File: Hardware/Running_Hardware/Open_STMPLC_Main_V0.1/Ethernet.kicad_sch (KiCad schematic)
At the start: 16 parts, among them J1 RJ45_Bel_SI-60062-F, U1 LAN8720A

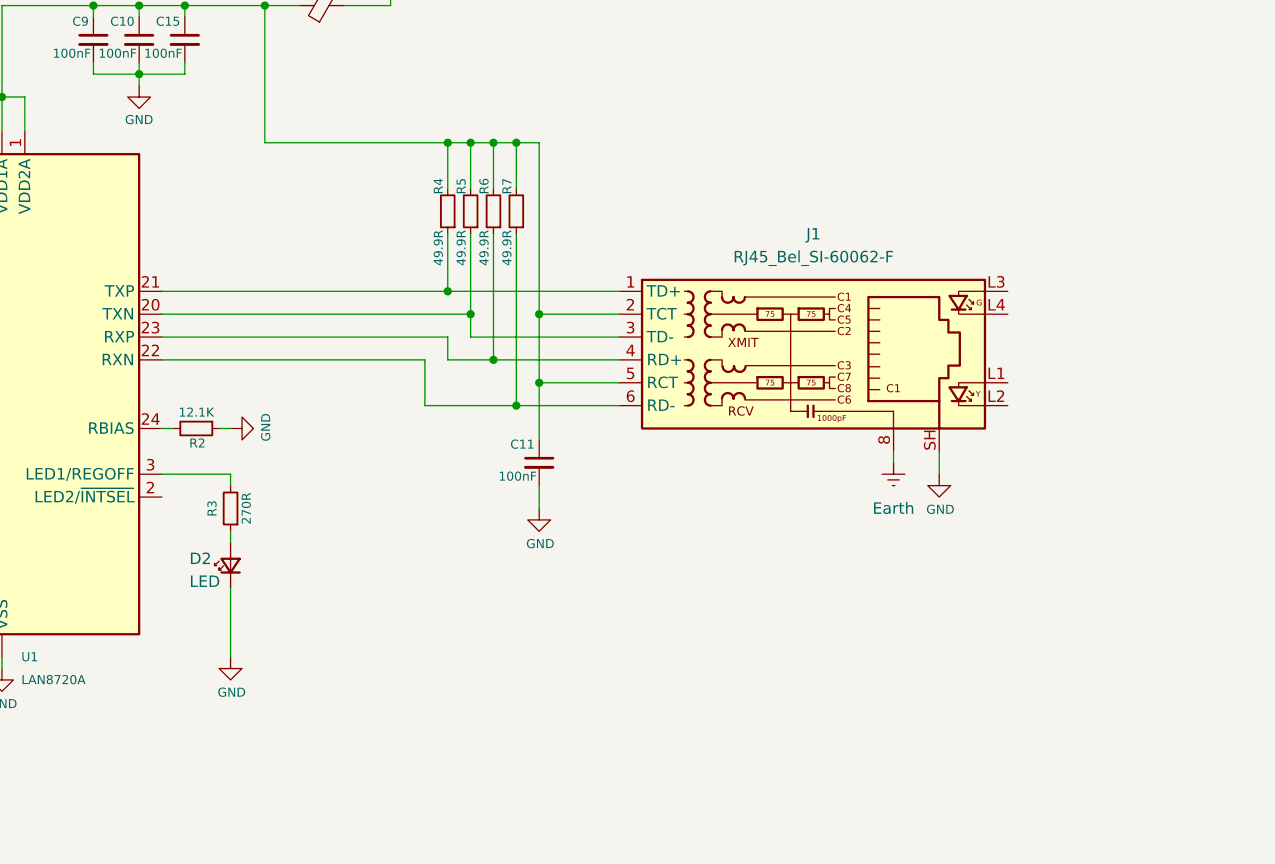
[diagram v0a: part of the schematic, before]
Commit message: GSM Module add
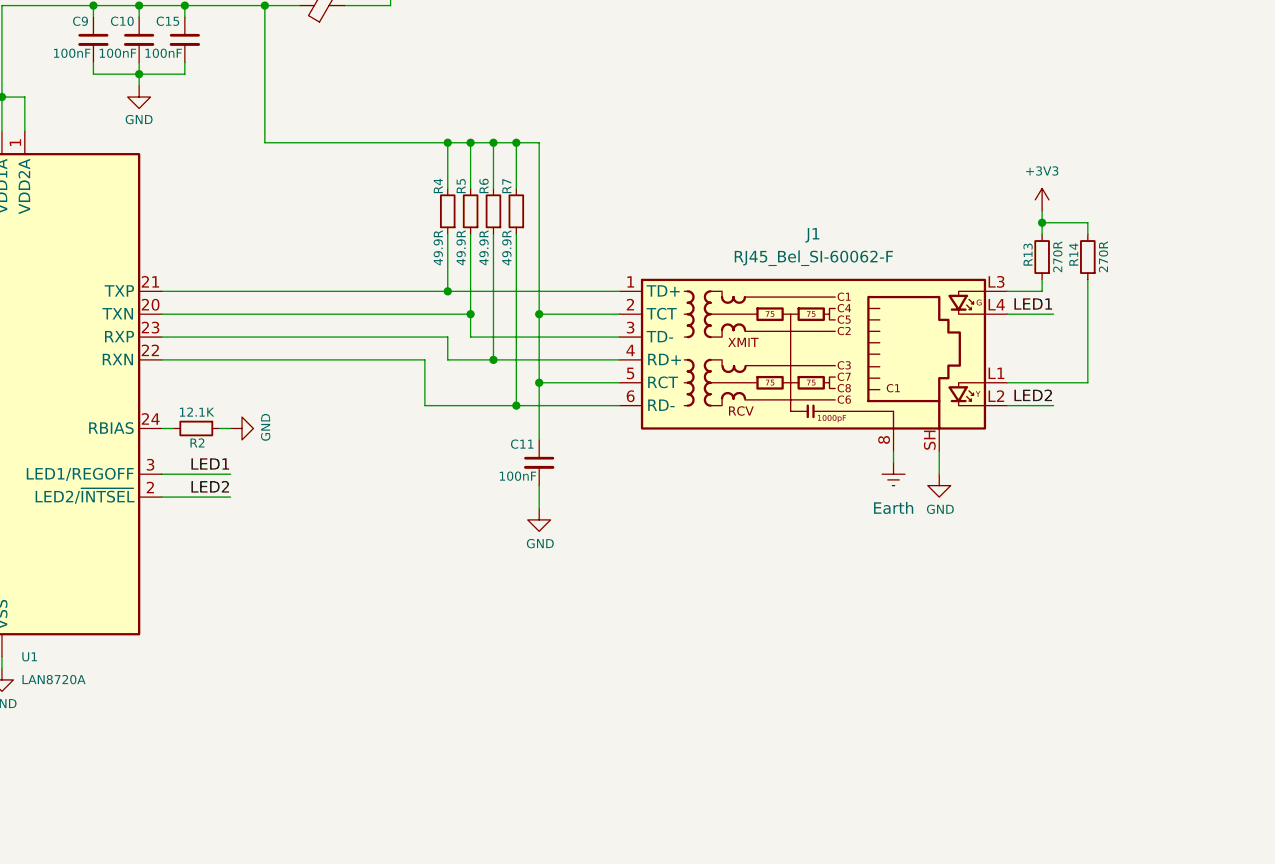
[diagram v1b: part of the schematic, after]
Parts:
- removed D2: LED, symbol Device:LED_Small
- removed R3: 270R, symbol Device:R_Small
- added R13, R14: 270R, Resistor_SMD:R_0603_1608Metric_Pad0.98x0.95mm_HandSolder, symbol Device:R_Small
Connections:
- net +3V3: now also R13.2, R14.2
- net at J1.L1: now also R14.1
- net LED2: now reaches J1.L2
- net LED2: now also U1.2 (LED2/~{INTSEL})
- net at J1.L3: now also R13.1
- net LED1: now reaches J1.L4
- net LED1: now also U1.3 (LED1/REGOFF)

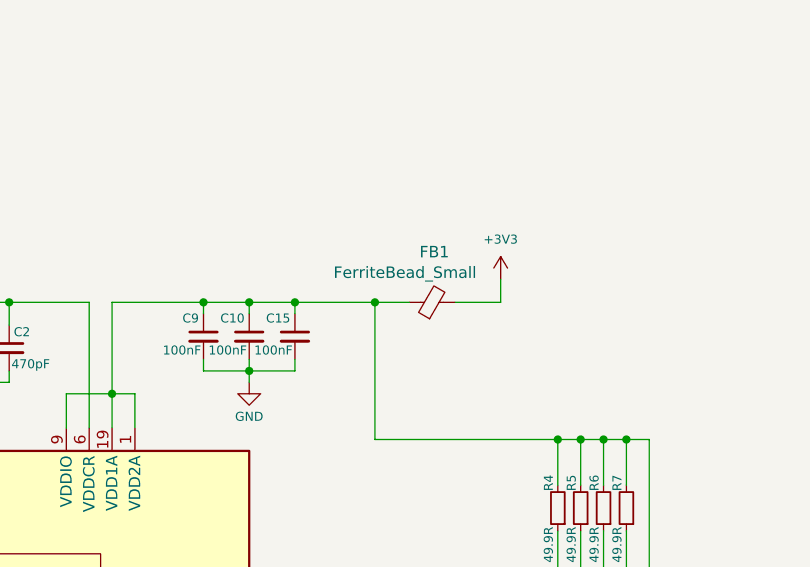
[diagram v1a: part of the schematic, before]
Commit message: Main PCB schematic changes V0.1
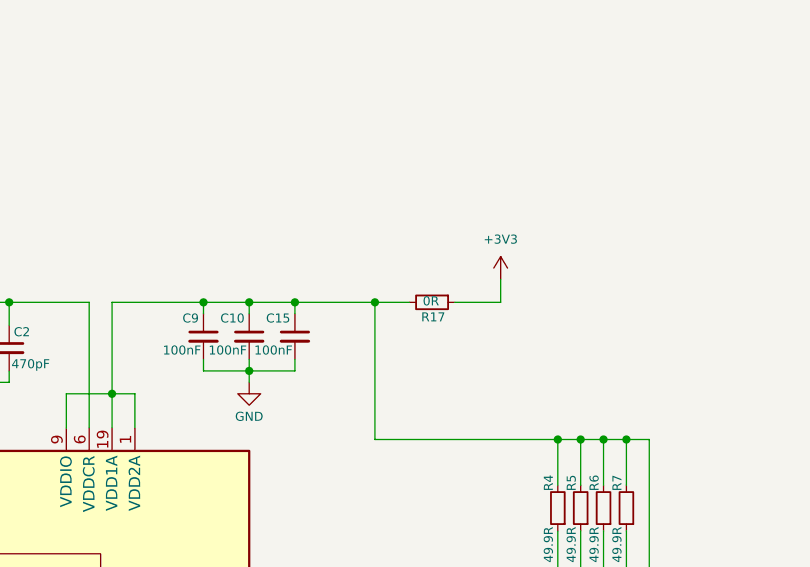
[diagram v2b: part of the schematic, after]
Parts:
- removed FB1: FerriteBead_Small, symbol Device:FerriteBead_Small
- added R17: 0R, Resistor_SMD:R_0603_1608Metric_Pad0.98x0.95mm_HandSolder, symbol Device:R_Small
- C2, C8: footprint (none) -> Capacitor_SMD:C_0603_1608Metric_Pad1.08x0.95mm_HandSolder
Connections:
- net +3V3: now also R17.1
- net at C10.1, C11.1, C15.1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: now also R17.2
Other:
- title: (none) -> Open_STMPLC_Main
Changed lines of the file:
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@@
 	(generator_version "9.0")
 	(paper "A4")
+	(title_block
+		(title "Open_STMPLC_Main")
+		(date "2026-04-04")
+		(rev "0.1")
+	)
 	(rectangle
 		(start 13.97 13.97)
@@
 			)
 		)
-		(property "Footprint" ""
+		(property "Footprint" "Capacitor_SMD:C_0603_1608Metric_Pad1.08x0.95mm_HandSolder"
 			(at 95.25 59.69 0)
 			(effects
@@
 	(symbol
 		(lib_id "Device:R_Small")
+		(at 147.32 54.61 270)
+		(unit 1)
+		(exclude_from_sim no)
+		(in_bom yes)
+		(on_board yes)
+		(dnp no)
+		(property "Reference" "R17"
+			(at 147.447 56.261 90)
+			(effects
+				(font
+					(size 1 1)
+				)
+			)
+		)
+		(property "Value" "0R"
+			(at 147.193 54.483 90)
+			(effects
+				(font
+					(size 1 1)
+				)
+			)
+		)
+		(property "Footprint" "Resistor_SMD:R_0603_1608Metric_Pad0.98x0.95mm_HandSolder"
+			(at 147.32 54.61 0)
+			(effects
+				(font
+					(size 1.27 1.27)
+				)
+				(hide yes)
+			)
+		)
+		(property "Datasheet" "~"
+			(at 147.32 54.61 0)
+			(effects
+				(font
+					(size 1.27 1.27)
+				)
+				(hide yes)
+			)
+		)
+		(property "Description" "Resistor, small symbol"
+			(at 147.32 54.61 0)
+			(effects
+				(font
+					(size 1.27 1.27)
+				)
+				(hide yes)
+			)
+		)
+		(pin "2"
+		)
+		(pin "1"
+		)
+		(instances
+			(project "Open_STMPLC_Main_V0.1"
+				(path "/0b17c9ff-697e-478a-b9b2-a0c5b14c9e6c/2c4ca765-43c3-4f95-8835-dba7f06999bb"
+					(reference "R17")
+					(unit 1)
+				)
+			)
+		)
+	)
+	(symbol
+		(lib_id "Device:R_Small")
 		(at 161.29 77.47 180)
 		(unit 1)
@@
 			)
 		)
-		(property "Footprint" ""
+		(property "Footprint" "Capacitor_SMD:C_0603_1608Metric_Pad1.08x0.95mm_HandSolder"
 			(at 100.33 59.69 0)
 			(effects
@@
 					(unit 1)
 				)
-			)
-		)
-	)
-	(symbol
-		(lib_id "Device:FerriteBead_Small")
-		(at 147.32 54.61 90)
-		(unit 1)
-		(exclude_from_sim no)
-		(in_bom yes)
-		(on_board yes)
-		(dnp no)
-		(property "Reference" "FB1"
-			(at 147.574 49.022 90)
-			(effects
-				(font
-					(size 1.27 1.27)
-				)
-			)
-		)
-		(property "Value" "FerriteBead_Small"
-			(at 144.3101 51.308 90)
-			(effects
-				(font
-					(size 1.27 1.27)
-				)
-			)
-		)
-		(property "Footprint" ""
-			(at 147.32 56.388 90)
-			(effects
-				(font
-					(size 1.27 1.27)
-				)
-				(hide yes)
-			)
-		)
-		(property "Datasheet" "~"
-			(at 147.32 54.61 0)
-			(effects
-				(font
-					(size 1.27 1.27)
-				)
-				(hide yes)
-			)
-		)
-		(property "Description" "Ferrite bead, small symbol"
-			(at 147.32 54.61 0)
-			(effects
-				(font
-					(size 1.27 1.27)
-				)
-				(hide yes)
-			)
-		)
-		(pin "1"
-		)
-		(pin "2"
-		)
-		(instances
-			(project "Open_STMPLC_Main_V0.1"
-				(path "/0b17c9ff-697e-478a-b9b2-a0c5b14c9e6c/2c4ca765-43c3-4f95-8835-dba7f06999bb"
-					(reference "FB1")
-					(unit 1)
-				)

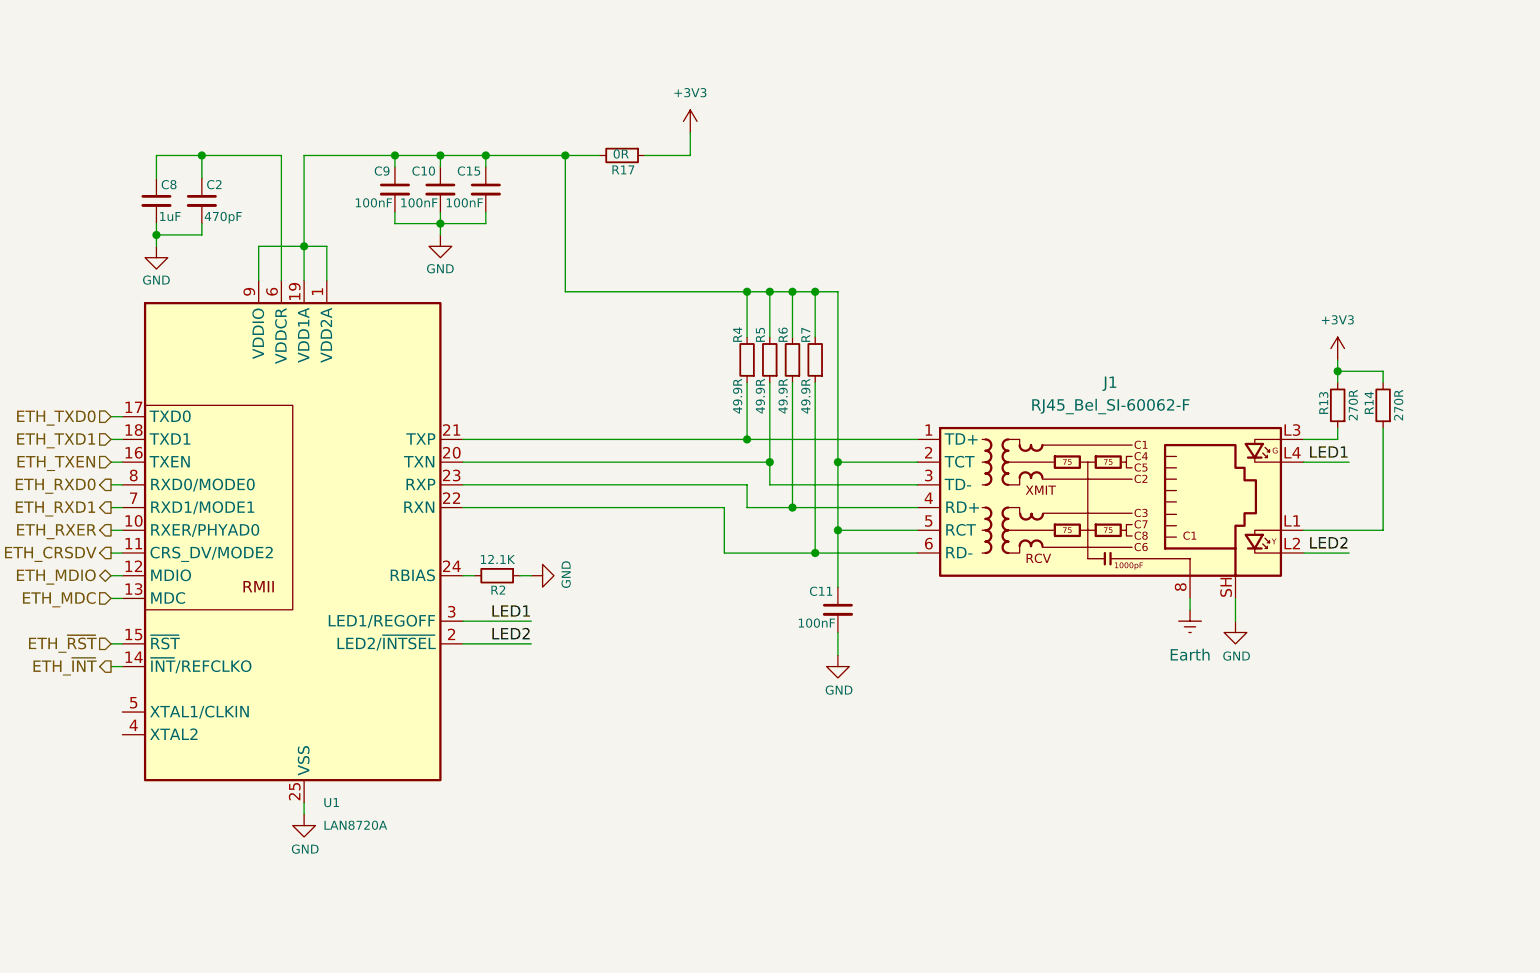
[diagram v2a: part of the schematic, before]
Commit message: Pin mapping IO connector
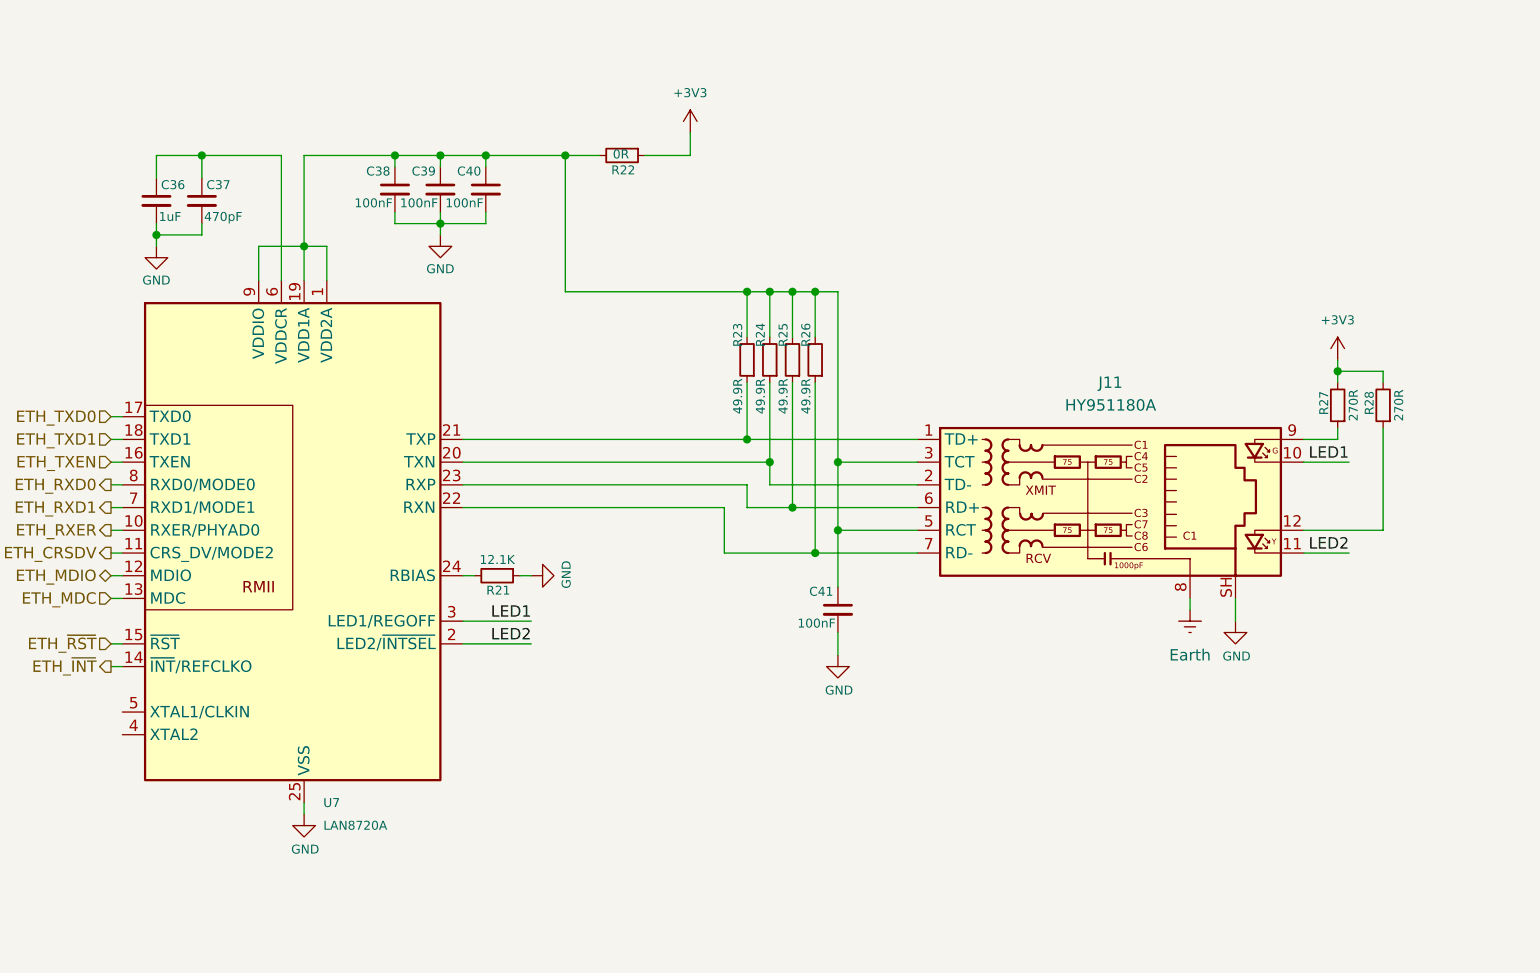
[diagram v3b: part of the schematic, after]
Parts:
- removed J1: RJ45_Bel_SI-60062-F, Connector_RJ:RJ45_Bel_SI-60062-F, symbol Connector:RJ45_Bel_SI-60062-F
- added J11: HY951180A, HY951180A:HY951180A, symbol HY951180A:HY951180A
- renumbered C8 to C36, C2 to C37, C9 to C38, C10 to C39, C15 to C40, C11 to C41, R2 to R21, R17 to R22, R4 to R23, R5 to R24, R6 to R25, R7 to R26, R13 to R27, R14 to R28, U1 to U7
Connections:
- net Earth: now also J11.8
- net GND: now also J11.SH
- net LED1: now also J11.10
- net LED2: now also J11.11
- net at C38.1, C39.1, C40.1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: now also J11.3 (TCT), J11.5 (RCT)
- net at R28.1: now also J11.12
- net at R23.1, U7.21 (TXP): now also J11.1 (TD+)
- net at R24.1, U7.20 (TXN): now also J11.2 (TD-)
- net at R25.1, U7.23 (RXP): now also J11.6 (RD+)
- net at R26.1, U7.22 (RXN): now also J11.7 (RD-)
- net at R27.1: now also J11.9

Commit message: Main PCB changes
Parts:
- added C57, C58: 10pF, Capacitor_SMD:C_0603_1608Metric_Pad1.08x0.95mm_HandSolder, symbol Device:C_Small
- added Y3: 25MHz, Crystal:Crystal_SMD_5032-4Pin_5.0x3.2mm, symbol Device:Crystal_GND24
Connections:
- net GND: now also C57.2, C58.2, Y3.2, Y3.4
- net at U7.4 (XTAL2): now also C58.1, Y3.1
- net at U7.5 (XTAL1/CLKIN): now also C57.1, Y3.3
